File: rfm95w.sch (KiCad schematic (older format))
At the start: 3 parts, among them J2 5-1814400-1, U3 RFM95W-915S2

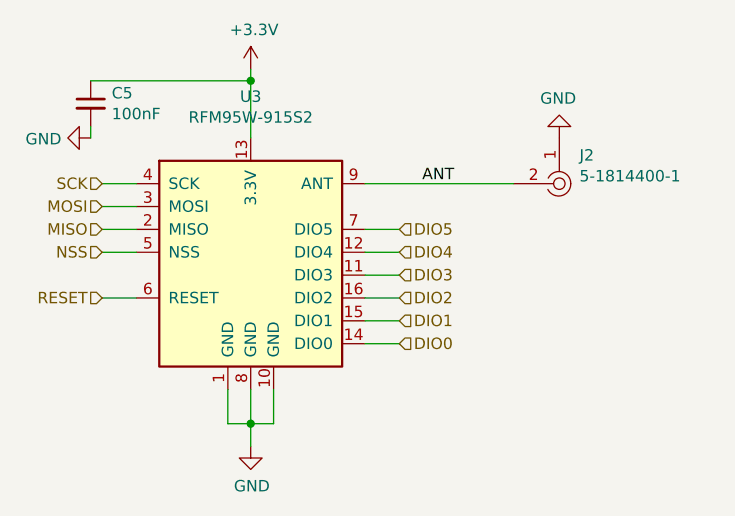
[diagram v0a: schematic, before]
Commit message: Roteamento da PCB pronto; Agora o 3v3 da raspberry alimenta os resistores de pull up da comunicacao i2c do bq24160
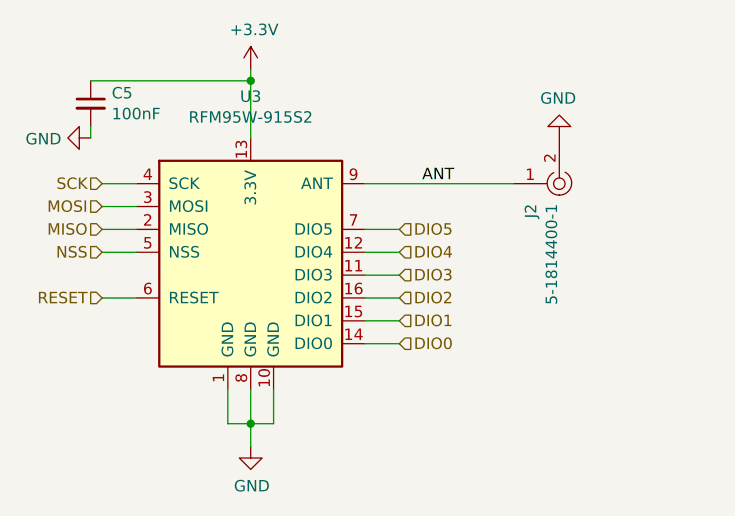
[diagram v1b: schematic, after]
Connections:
- net ANT: now also J2.1; no longer J2.2
- net GND: now also J2.2; no longer J2.1
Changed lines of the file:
@@
 F 12 "Active" H 6800 4900 60  0001 L CNN "Status"
 	1    6600 3700
-	-1   0    0    1
+	0    1    -1   0
 $EndComp
 $Comp

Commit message: Roteamento completo. Aprovado pelo professor Claudinei.
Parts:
- U3: footprint RF_Module:HOPERF_RFM9XW_THT -> RF_Module:HOPERF_RFM9XW_SMD
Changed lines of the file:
@@
 F 0 "U3" H 5250 4681 50  0000 C CNN
 F 1 "RFM95W-915S2" H 5250 4590 50  0000 C CNN
-F 2 "RF_Module:HOPERF_RFM9XW_THT" H 1950 5650 50  0001 C CNN
+F 2 "RF_Module:HOPERF_RFM9XW_SMD" H 1950 5650 50  0001 C CNN
 F 3 "https://www.hoperf.com/data/upload/portal/20181127/5bfcbea20e9ef.pdf" H 1950 5650 50  0001 C CNN
 	1    5250 4000

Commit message: v3
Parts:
- renumbered J2 to J1, U3 to U4
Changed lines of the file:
@@
 $Descr A4 11693 8268
 encoding utf-8
-Sheet 4 7
+Sheet 3 7
 Title ""
 Date ""
@@
 $EndDescr
 $Comp
-L RF_Module:RFM95W-915S2 U3
+L RF_Module:RFM95W-915S2 U4
 U 1 1 61DA8ABC
 P 5250 4000
-F 0 "U3" H 5250 4681 50  0000 C CNN
+F 0 "U4" H 5250 4681 50  0000 C CNN
 F 1 "RFM95W-915S2" H 5250 4590 50  0000 C CNN
 F 2 "RF_Module:HOPERF_RFM9XW_SMD" H 1950 5650 50  0001 C CNN
@@
 $EndComp
 $Comp
-L power:GND #PWR0114
+L power:GND #PWR012
 U 1 1 61DA932B
 P 5250 4850
-F 0 "#PWR0114" H 5250 4600 50  0001 C CNN
+F 0 "#PWR012" H 5250 4600 50  0001 C CNN
 F 1 "GND" H 5255 4677 50  0000 C CNN
 F 2 "" H 5250 4850 50  0001 C CNN
@@
 	5250 4850 5250 4750
 $Comp
-L power:+3.3V #PWR0115
+L power:+3.3V #PWR011
 U 1 1 61DA96FA
 P 5250 3200
-F 0 "#PWR0115" H 5250 3050 50  0001 C CNN
+F 0 "#PWR011" H 5250 3050 50  0001 C CNN
 F 1 "+3.3V" H 5265 3373 50  0000 C CNN
 F 2 "" H 5250 3200 50  0001 C CNN
@@
 	5250 3250 5250 3500
 $Comp
-L power:GND #PWR0116
+L power:GND #PWR010
 U 1 1 61DAE92A
 P 4550 3500
-F 0 "#PWR0116" H 4550 3250 50  0001 C CNN
+F 0 "#PWR010" H 4550 3250 50  0001 C CNN
 F 1 "GND" V 4555 3372 50  0000 R CNN
 F 2 "" H 4550 3500 50  0001 C CNN
@@
 ANT
 $Comp
-L dk_Coaxial-Connectors-RF:5-1814400-1 J2
+L dk_Coaxial-Connectors-RF:5-1814400-1 J1
 U 1 1 61E0F67C
 P 6600 3700
-F 0 "J2" H 6512 3576 50  0000 R CNN
+F 0 "J1" H 6512 3576 50  0000 R CNN
 F 1 "5-1814400-1" H 6512 3667 50  0000 R CNN
 F 2 "digikey-footprints:RF_SMA_RightAngle_5-1814400-1" H 6800 3900 60  0001 L CNN
@@
 $EndComp
 $Comp
-L power:GND #PWR0117
+L power:GND #PWR013
 U 1 1 61E1056F
 P 6600 3500
-F 0 "#PWR0117" H 6600 3250 50  0001 C CNN
+F 0 "#PWR013" H 6600 3250 50  0001 C CNN
 F 1 "GND" H 6605 3327 50  0000 C CNN
 F 2 "" H 6600 3500 50  0001 C CNN
